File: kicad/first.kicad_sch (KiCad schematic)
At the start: 95 parts, among them J1 Conn_01x04_Pin, P1 USB_C_Plug_USB2.0, Q1 MMUN2111LT1G, Q2 MMBT3904, Q3 MMUN2111LT1G, Q4 MMBT3904, SW1 SW_SPDT, SW2 RotaryEncoder_Switch_MP, SW3 RotaryEncoder_Switch_MP, SW4 RotaryEncoder_Switch_MP, U1 STM32F407VETx, U2 LP5907MFX-3.3, U3 CS4272, U4 NE5532, U5 NE5532, U6 NE5532, U7 NE5532, Y1 X MHz

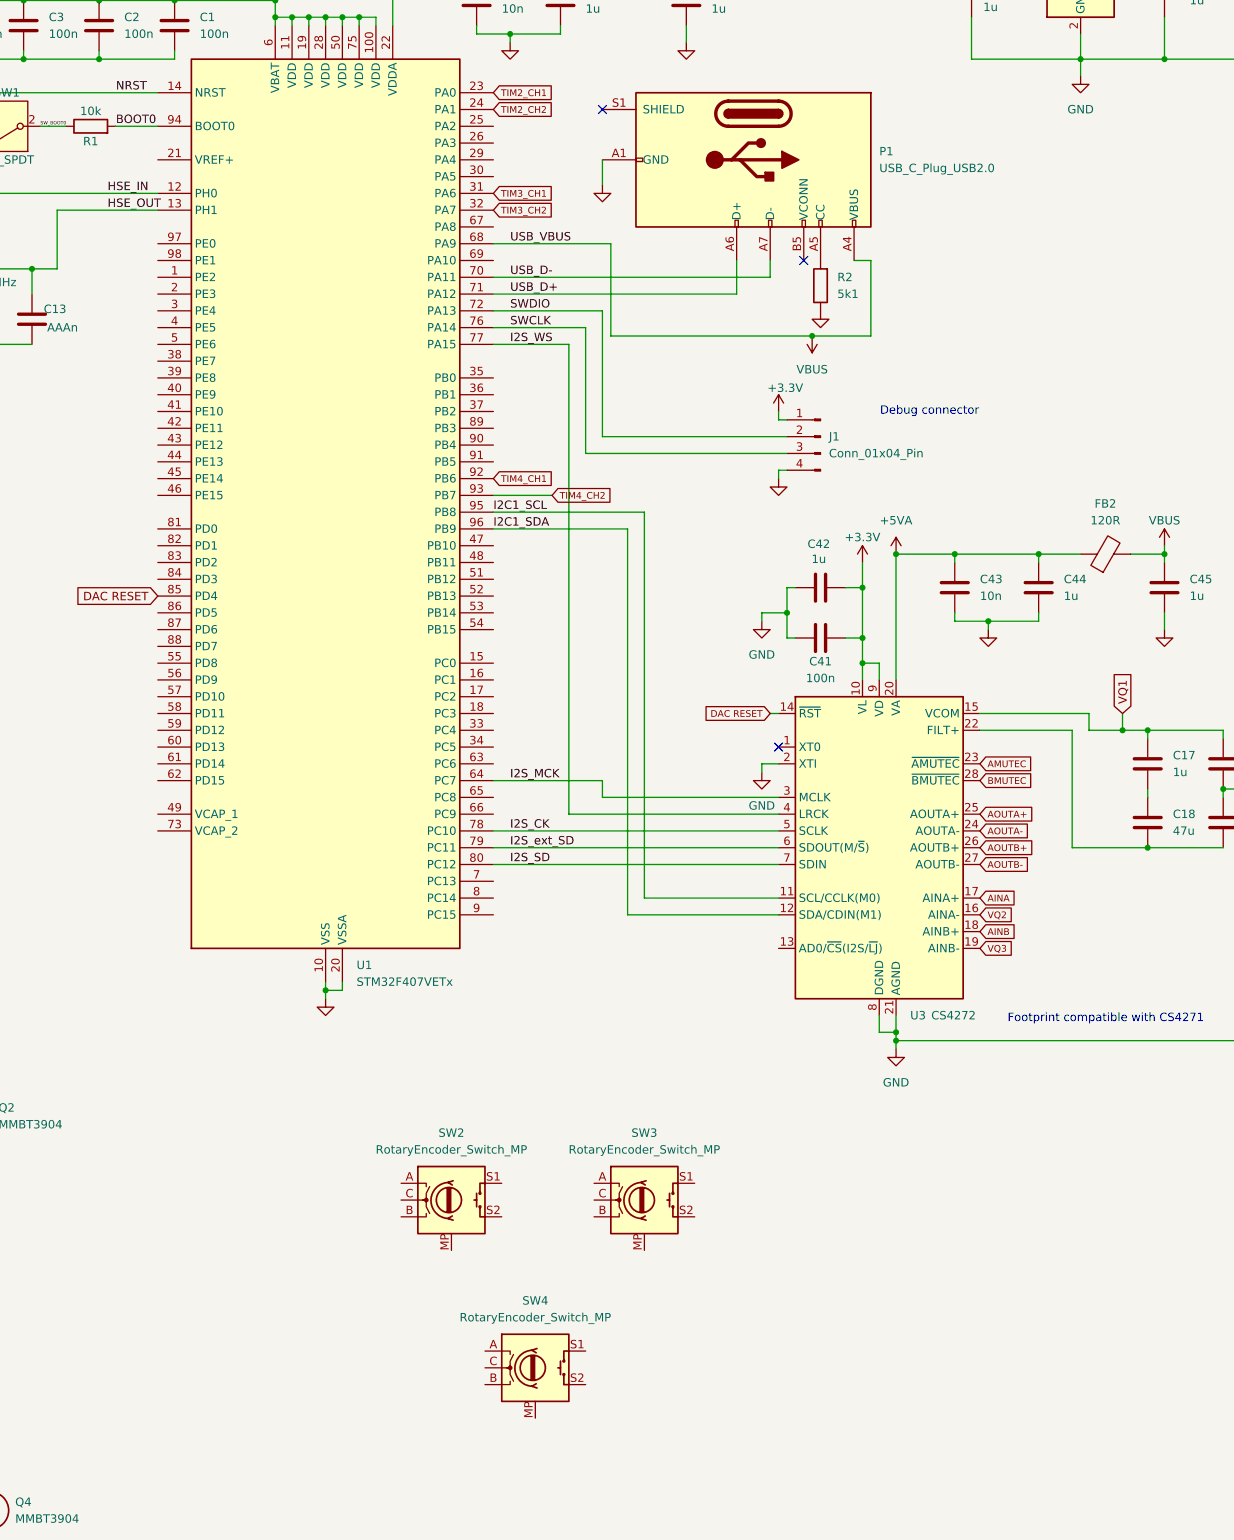
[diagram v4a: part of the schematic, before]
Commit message: encoder circuits, TIM and encoder switch connections
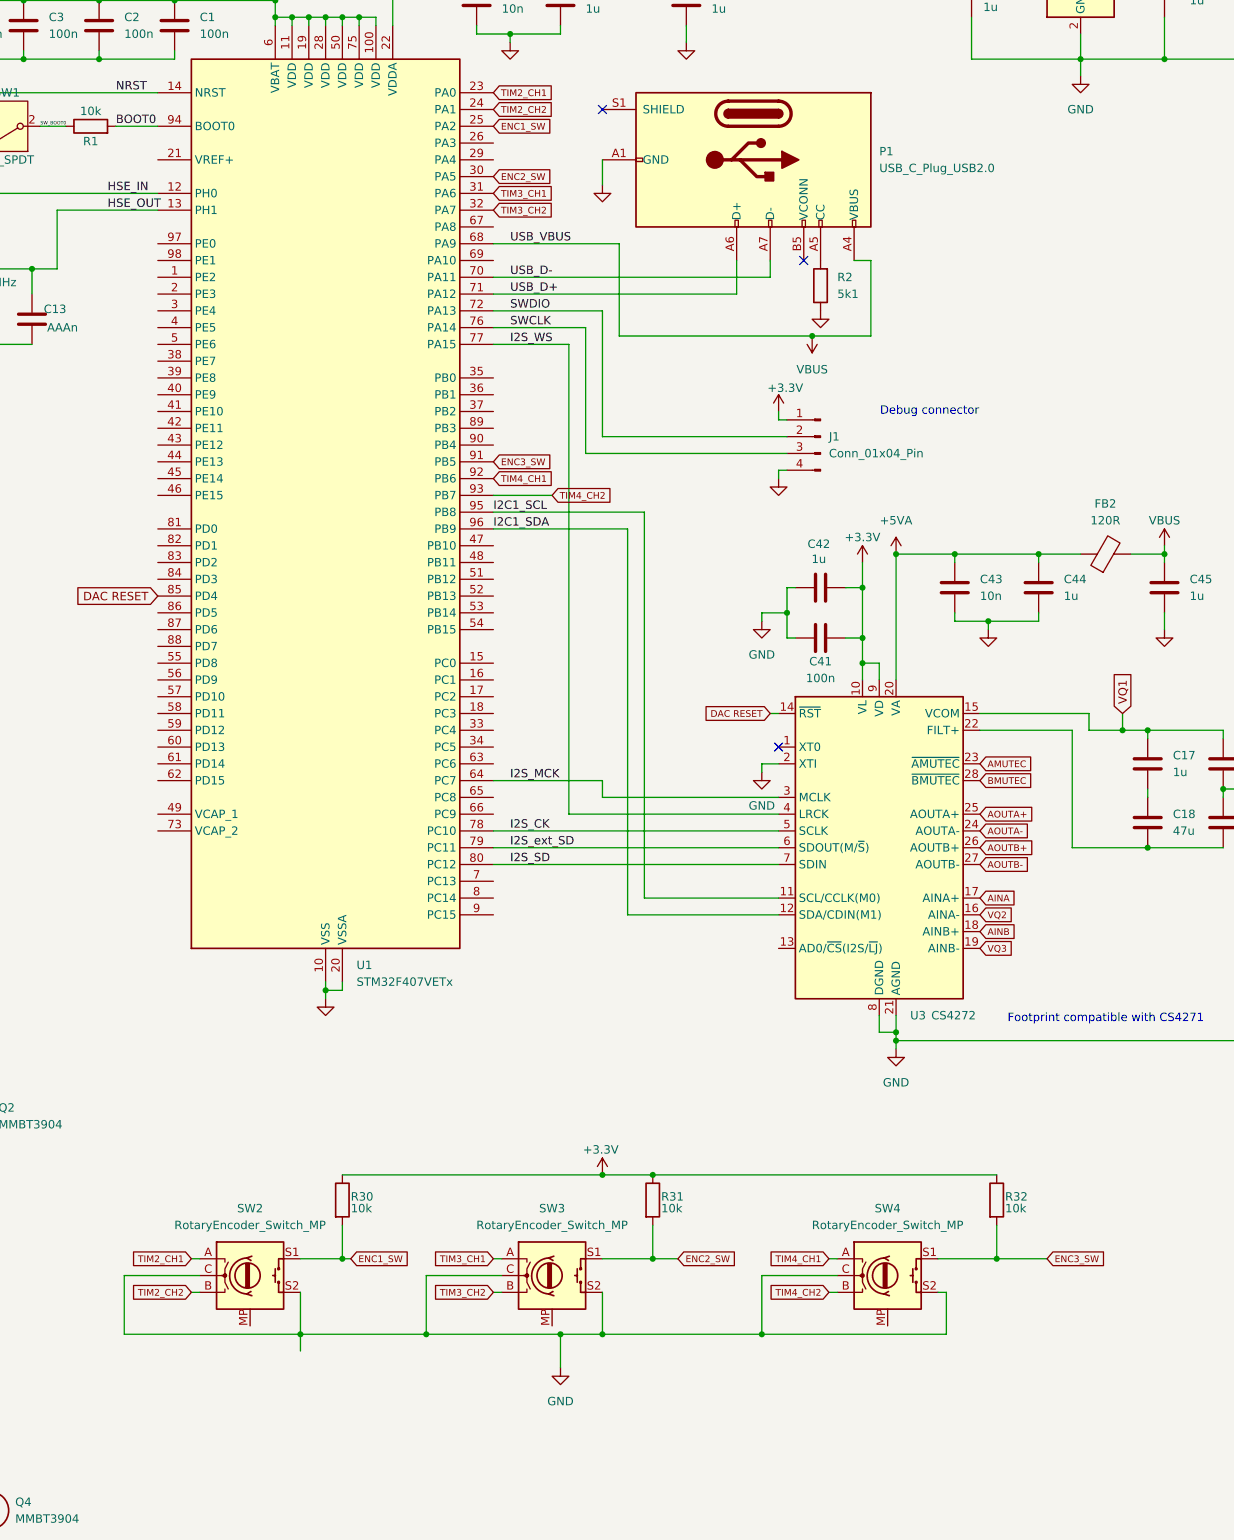
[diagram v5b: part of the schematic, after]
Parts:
- added R30, R31, R32: 10k, symbol Device:R
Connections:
- net +3.3V: now also R30.1, R31.1, R32.1
- net GND: now also SW2.C, SW2.S2, SW3.C, SW3.S2, SW4.C, SW4.S2
- net TIM2_CH1: now also SW2.A
- net TIM2_CH2: now also SW2.B
- net TIM3_CH1: now also SW3.A
- net TIM3_CH2: now also SW3.B
- net TIM4_CH1: now also SW4.A
- net TIM4_CH2: now also SW4.B
- net ENC2_SW: now reaches SW3.S1
- net ENC2_SW: now also U1.30 (PA5), R31.2
- net ENC1_SW: now reaches SW2.S1
- net ENC1_SW: now also U1.25 (PA2), R30.2
- net ENC3_SW: now reaches SW4.S1
- net ENC3_SW: now also U1.91 (PB5), R32.2
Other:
- moved on the sheet: SW2, SW3, SW4

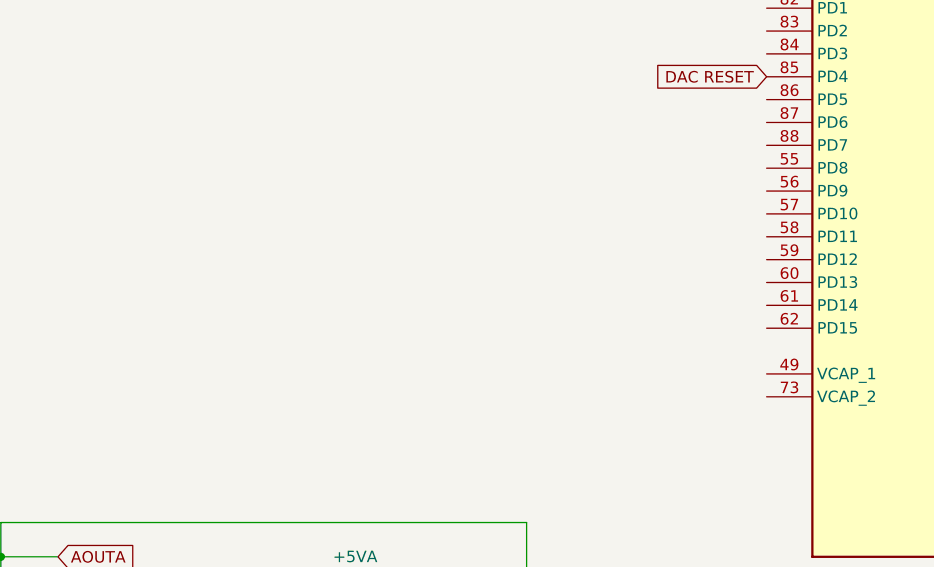
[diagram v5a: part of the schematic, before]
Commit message: added LED's for encoders
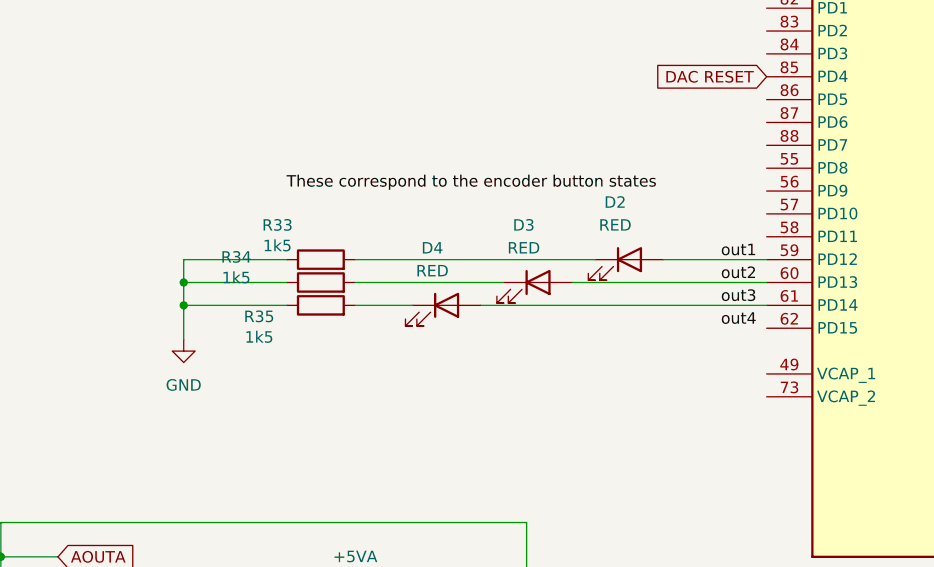
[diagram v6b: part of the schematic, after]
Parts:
- added D2, D3, D4: RED, symbol Device:LED
- added R33, R34, R35: 1k5, symbol Device:R
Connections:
- net GND: now also R33.1, R34.1, R35.1
- net out1: now reaches U1.59 (PD12)
- net out1: now also D2.2 (A)
- net out2: now reaches U1.60 (PD13)
- net out2: now also D3.2 (A)
- net out3: now reaches U1.61 (PD14)
- net out3: now also D4.2 (A)
- new net: D3.1 (K), R34.2
- new net: D2.1 (K), R33.2
- new net: D4.1 (K), R35.2

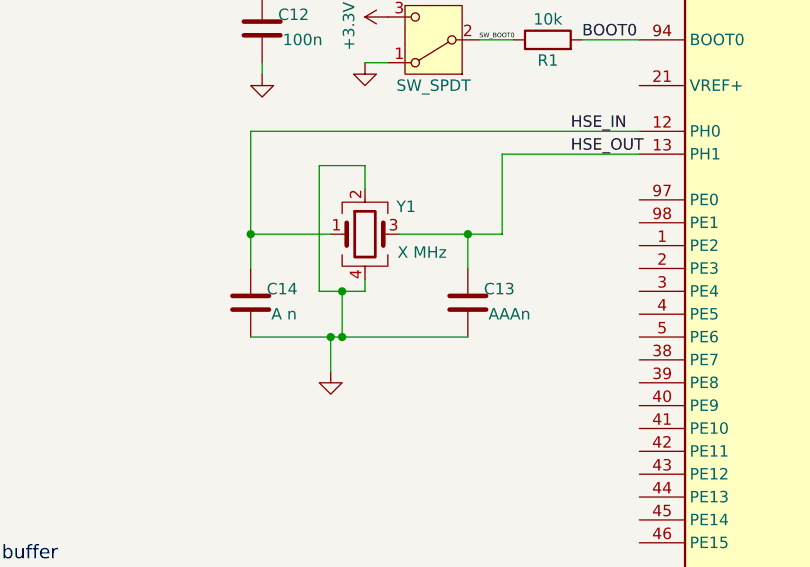
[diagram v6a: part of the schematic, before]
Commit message: new kicad version introduced some files. HSE circuit done
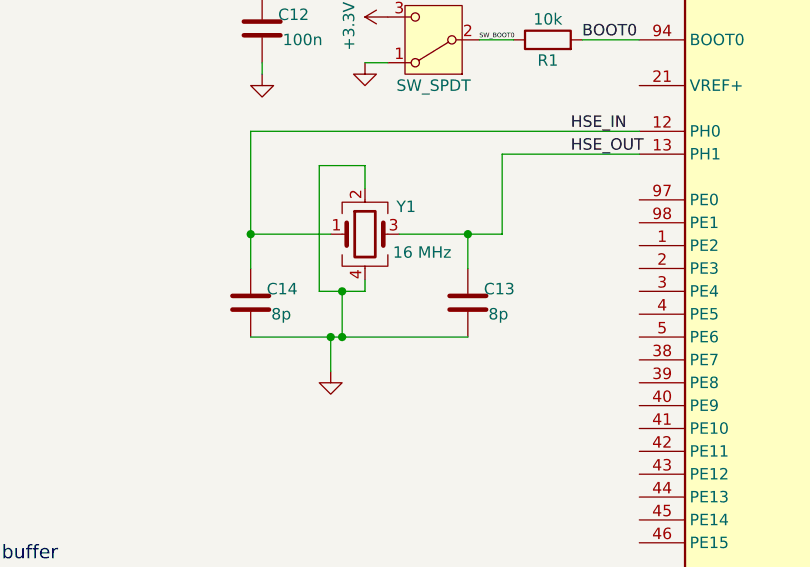
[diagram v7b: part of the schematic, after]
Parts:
- C13: value AAAn -> 8p
- C14: value A n -> 8p
- Y1: value X MHz -> 16 MHz

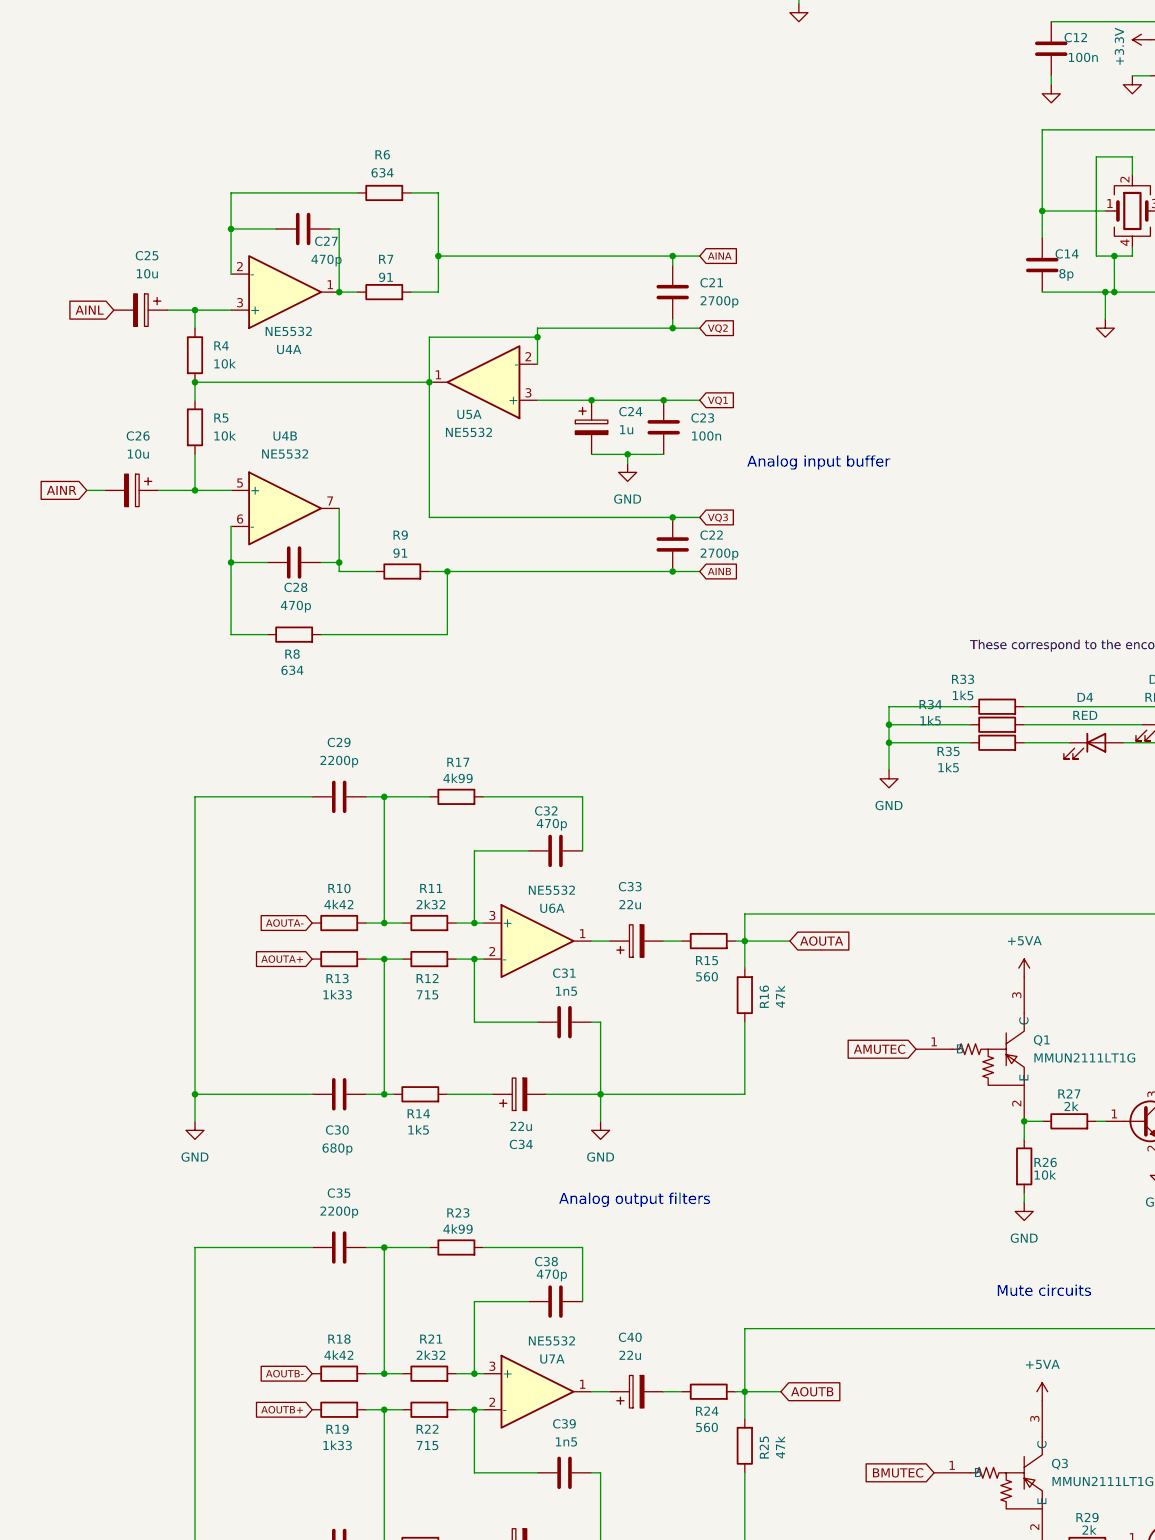
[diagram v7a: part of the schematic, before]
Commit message: hierarchy layer for inputs. Replaced input impedance with 1MOhm. Swapped NE5532 for wide supply range OP amp
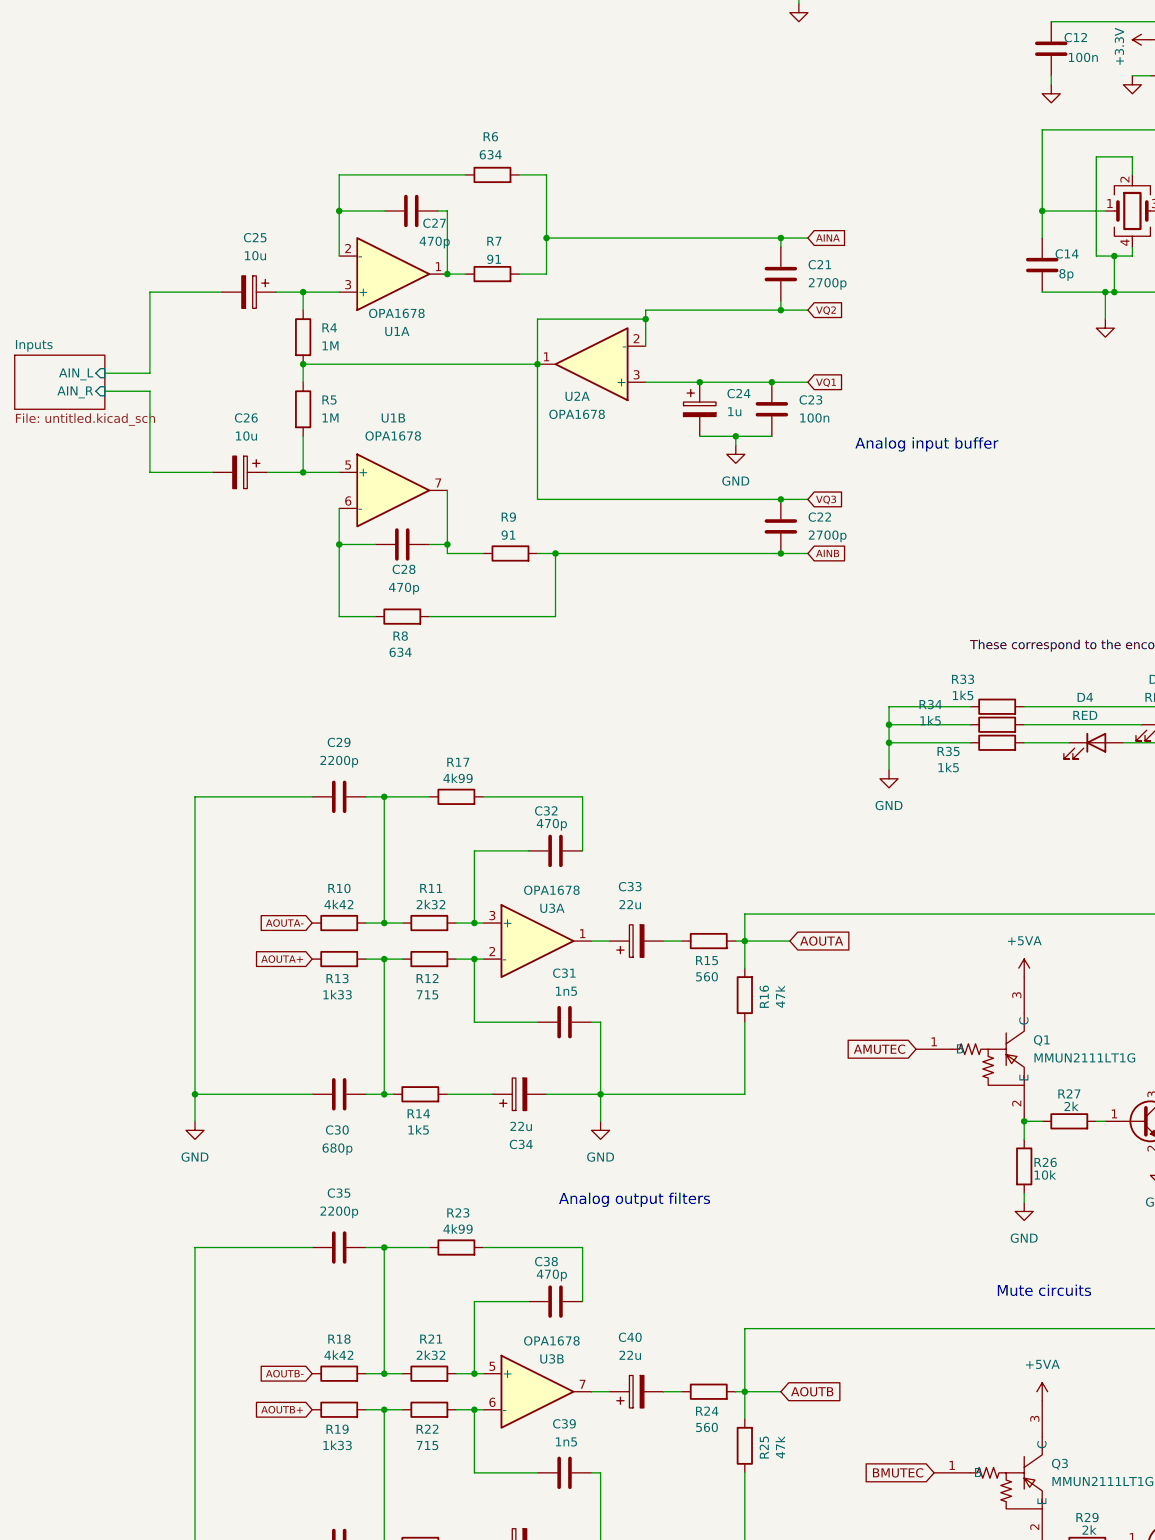
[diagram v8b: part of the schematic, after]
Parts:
- R4, R5: value 10k -> 1M
- U1: renamed from U4; value NE5532 -> OPA1678; footprint Package_SO:SOIC-8_5.3x6.2mm_P1.27mm -> Package_SO:SOIC-8_3.9x4.9mm_P1.27mm
- U2: renamed from U5; value NE5532 -> OPA1678; footprint Package_SO:SOIC-8_5.3x6.2mm_P1.27mm -> Package_SO:SOIC-8_3.9x4.9mm_P1.27mm
- U3: renamed from U6; value NE5532 -> OPA1678; footprint Package_SO:SOIC-8_5.3x6.2mm_P1.27mm -> Package_SO:SOIC-8_3.9x4.9mm_P1.27mm
- U3: renamed from U7; value NE5532 -> OPA1678; footprint Package_SO:SOIC-8_5.3x6.2mm_P1.27mm -> Package_SO:SOIC-8_3.9x4.9mm_P1.27mm
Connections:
- net at C38.2, R21.2: now also U3.5 (+); no longer U3.3 (+)
- net at C39.2, R22.2: now also U3.6 (-); no longer U3.2 (-)
- net at C40.1: now also U3.7; no longer U3.1
- net AINL renamed Inputs/AIN_L
- net AINR renamed Inputs/AIN_R
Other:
- added sheet Inputs (untitled.kicad_sch)
- moved on the sheet: C21, C22, C23, C24, C25, C26, C27, C28, R4, R5, R6, R7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
